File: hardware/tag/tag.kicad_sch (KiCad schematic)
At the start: 108 parts, among them J1 USB_C_Receptacle_USB2.0_16P, J2 BATTERY, J3 UART, J4 I2C, J5 STM SWD, J7 BLE SWD, J8 SOURCE, SW1 RESET, SW2 BOOT, SW3 USER, U1 ICM-45686, U2 TPS63070RNMR, U3 BQ24075RGT, U4 USBLC6-2SC6, U5 FSC-BT630, U6 STM32F411CEUx, U7 DWM1000, Y1 NX3215SA-32.768kHz(DNP), Y2 NX3225SA-24MHz

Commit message: refactor(hw): iterate on tag rev 0.2 design
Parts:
- removed C15: DNP, Capacitor_SMD:C_0805_2012Metric_Pad1.18x1.45mm_HandSolder, symbol Device:C
- removed C5: 1u, Capacitor_SMD:C_0805_2012Metric_Pad1.18x1.45mm_HandSolder, symbol Device:C
- removed C6, C7: 4.7u, Capacitor_SMD:C_0805_2012Metric_Pad1.18x1.45mm_HandSolder, symbol Device:C
- removed D1: RED, LED_SMD:LED_0603_1608Metric_Pad1.05x0.95mm_HandSolder, symbol Device:LED
- removed D2: YELLOW, LED_SMD:LED_0603_1608Metric_Pad1.05x0.95mm_HandSolder, symbol Device:LED
- removed R18, R9: 6k, Resistor_SMD:R_0603_1608Metric_Pad0.98x0.95mm_HandSolder, symbol Device:R
- removed R8: 10k, Resistor_SMD:R_0603_1608Metric_Pad0.98x0.95mm_HandSolder, symbol Device:R
- removed SW2: BOOT, Button_Switch_SMD:SW_SPDT_PCM12, symbol Switch:SW_SPDT
- removed U3: BQ24075RGT, Package_DFN_QFN:VQFN-16-1EP_3x3mm_P0.5mm_EP1.6x1.6mm, symbol Battery_Management:BQ24075RGT
- removed U5: FSC-BT630, Other_Footprint:FSC-BT630, symbol FSC-BT630_Generic_20P:FSC-BT630_Named_20P
- added C10: 1u, Capacitor_SMD:C_0805_2012Metric_Pad1.18x1.45mm_HandSolder, symbol Device:C
- added C12, C8: DNP, Capacitor_SMD:C_01005_0402Metric, symbol Device:C_Small
- added C34: 47n, Capacitor_SMD:C_0603_1608Metric, symbol Device:C_Small
- added C35: 4.7u, Capacitor_SMD:C_0805_2012Metric, symbol Device:C_Small
- added C36: 20u, Capacitor_SMD:C_0805_2012Metric, symbol Device:C
- added C37: 10u, Capacitor_SMD:C_0805_2012Metric, symbol Device:C
- added D9: YELLOW, LED_SMD:LED_0603_1608Metric_Pad1.05x0.95mm_HandSolder, symbol Device:LED
- added J6: BLE_Conn, Connector_Coaxial:U.FL_Hirose_U.FL-R-SMT-1_Vertical, symbol Connector:Conn_Coaxial_Small
- added L2: DNP, Inductor_SMD:L_0402_1005Metric, symbol Device:L
- added L3: 1u, Inductor_SMD:L_Sunlord_SWPA4020S, symbol Device:L
- added R25: 2.2k, Resistor_SMD:R_0603_1608Metric_Pad0.98x0.95mm_HandSolder, symbol Device:R
- added R26: 10K, Resistor_SMD:R_0603_1608Metric_Pad0.98x0.95mm_HandSolder, symbol Device:R
- added R27: DNP, Resistor_SMD:R_0603_1608Metric_Pad0.98x0.95mm_HandSolder, symbol Device:R
- added SW2: PWR, Button_Switch_SMD:SW_Push_1P1T-MP_NO_Horizontal_Alps_SKRTLAE010, symbol Switch:SW_Push
- added U5: FSC-BT630, other_footprint:FSC-BT630, symbol FSC-BT630:FSC-BT630_Named_20P
- added U8: BQ25628RYKR, Other_Footprint:IC_BQ25628RYKR, symbol BQ25628RYKR:BQ25628RYKR
- D3: value YELLOW -> GREEN
- D4: value GREEN -> RED
- R2: value 3.1k -> 10k
- R3: value 3.56k -> 10k
- renumbered C14 to C15
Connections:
- net +3.3V: now also R2.1, R3.1, U5.7 (VDD)
- net +BATT: now also C37.1, U8.8 (BAT)
- net BLE_RST: now also U5.6 (RESET)
- net BLE_RX: now also U5.1 (UART_TX)
- net BLE_SWDCLK: now also U5.9 (SWDCLK)
- net BLE_SWDIO: now also U5.10 (SWDIO)
- net BLE_TX: now also U5.2 (UART_RX)
- net GND: now also R14.1, C10.1, C12.2, C35.2, C36.2, C37.2, C8.2, D9.1 (K), J6.2 (Ext), R27.1, SW2.1, U5.19 (GND1), U5.8 (GND0), U8.14 (~{CE}), U8.15 (GND); no longer R2.2, R3.2
- net SYS: now also C36.1, L3.2, U8.9 (SYS)
- net VBUS: now also C10.2, U8.18 (VBUS)
- net at R19.2: now also U5.15 (P0.03)
- net PA15 / TIM2_CH1 renamed LED_PM
- net LED_PM: now also R25.2
- net PA8 / TIM1_CH1 renamed PM_SCL
- net PM_SCL: now also R2.2, U8.13 (SCL)
- net PB4/TIM3_CH1 renamed PM_SDA
- net PM_SDA: now also R3.2, U8.12 (SDA)
- net PB6 / TIM4_CH1: no longer names the net of U6.42 (PB6)
- new net: C8.1, J6.1 (In), L2.2
- new net: R26.1, SW2.2
- new net: R26.2, U8.7 (~{QON})
- new net: D9.2 (A), R25.1
- new net: R27.2, U8.4 (ILIM/D-)
- new net: C35.1, U8.2 (REGN)
- new net: C34.2, L3.1, U8.16 (SW)
- new net: C12.1, L2.1, U5.20 (EXT_ANT)
- new net: C34.1, U8.1 (BTST)
- new net STAT: U8.10 (STAT)
- new net TS: U8.5 (TS_BIAS/D+), U8.6 (TS)
- no-connect marks 31 -> 33
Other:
- note added: "PI Filter"
- note added: "TRACE 50 Ohm !"
- moved on the sheet: C16, C17, C18, C19, C20, C21, C22, C23, C24, C25, C26, C27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

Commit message: update(hw): release tag revision 0.2
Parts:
- removed C1: 10u, Capacitor_SMD:C_0805_2012Metric_Pad1.18x1.45mm_HandSolder, symbol Device:C
- removed C10: 1u, Capacitor_SMD:C_0805_2012Metric_Pad1.18x1.45mm_HandSolder, symbol Device:C
- removed C34: 47n, Capacitor_SMD:C_0603_1608Metric, symbol Device:C_Small
- removed C35: 4.7u, Capacitor_SMD:C_0805_2012Metric, symbol Device:C_Small
- removed C36: 20u, Capacitor_SMD:C_0805_2012Metric, symbol Device:C
- removed C37: 10u, Capacitor_SMD:C_0805_2012Metric, symbol Device:C
- removed L3: 1u, Inductor_SMD:L_Sunlord_SWPA4020S, symbol Device:L
- removed R2, R3: 10k, Resistor_SMD:R_0603_1608Metric_Pad0.98x0.95mm_HandSolder, symbol Device:R
- removed R27: DNP, Resistor_SMD:R_0603_1608Metric_Pad0.98x0.95mm_HandSolder, symbol Device:R
- removed SW2: PWR, Button_Switch_SMD:SW_Push_1P1T-MP_NO_Horizontal_Alps_SKRTLAE010, symbol Switch:SW_Push
- removed U8: BQ25628RYKR, Other_Footprint:IC_BQ25628RYKR, symbol BQ25628RYKR:BQ25628RYKR
- added C4: 100n, Capacitor_SMD:C_0603_1608Metric_Pad1.08x0.95mm_HandSolder, symbol Device:C
- added C6: 1u, Capacitor_SMD:C_0805_2012Metric_Pad1.18x1.45mm_HandSolder, symbol Device:C
- added C7: 1u, Capacitor_SMD:C_0603_1608Metric_Pad1.08x0.95mm_HandSolder, symbol Device:C
- added C8: 4.7u, Capacitor_SMD:C_0805_2012Metric_Pad1.18x1.45mm_HandSolder, symbol Device:C
- added C9: 10u, Capacitor_SMD:C_0805_2012Metric_Pad1.18x1.45mm_HandSolder, symbol Device:C
- added J9: I2C, Other_Footprint:JST_BM04B-SRSS-TB_LF__SN_, symbol BM04B-SRSS-TB_LF__SN_:BM04B-SRSS-TB_LF__SN_
- added Q1: AO664, Package_SO:TSOP-6_1.65x3.05mm_P0.95mm, symbol Transistor_FET:IRF7309PBF
- added R12: 100k, Resistor_SMD:R_0603_1608Metric_Pad0.98x0.95mm_HandSolder, symbol Device:R
- added R13, R8: 10k, Resistor_SMD:R_0603_1608Metric_Pad0.98x0.95mm_HandSolder, symbol Device:R
- added R5: 3.1k, Resistor_SMD:R_0603_1608Metric_Pad0.98x0.95mm_HandSolder, symbol Device:R
- added R6: 3.56k, Resistor_SMD:R_0603_1608Metric_Pad0.98x0.95mm_HandSolder, symbol Device:R
- added SW1: PWR, Button_Switch_SMD:SW_Push_1P1T-MP_NO_Horizontal_Alps_SKRTLAE010, symbol Switch:SW_Push_Shielded
- added U1: MAX17048G_T10, Package_SON:SON-8-1EP_3x2mm_P0.5mm_EP1.4x1.6mm, symbol MAX17048G_T10:MAX17048G_T10
- added U5: BQ24075RGT, Package_DFN_QFN:VQFN-16-1EP_3x3mm_P0.5mm_EP1.6x1.6mm, symbol Battery_Management:BQ24075RGT
- D3: value GREEN -> YELLOW
- D4: renamed from D9; value YELLOW -> GREEN
- D5: renamed from D4; value RED -> GREEN
- R14: value 10K -> 10k
- TP2: renamed from TP3; footprint TestPoint:TestPoint_Pad_D2.0mm -> TestPoint:TestPoint_Pad_1.5x1.5mm
- TP5: renamed from TP4; footprint TestPoint:TestPoint_Pad_D2.0mm -> TestPoint:TestPoint_Pad_1.5x1.5mm
- renumbered C2 to C1, C31 to C10, C13 to C12, C32 to C13, C15 to C14, C33 to C15, C27 to C16, C26 to C17, C16 to C18, C17 to C19, C3 to C2, C18 to C20, C19 to C21, C20 to C22, C21 to C23, C22 to C24, C12 to C25, C8 to C26, C23 to C27, C24 to C28, C25 to C29, C4 to C3, C28 to C30, C29 to C31, C30 to C32, C9 to C5, D7 to D1, D8 to D2, D5 to D6, D6 to D7, H3 to H1, H4 to H2, H2 to H3, H1 to H4, J6 to J3, J8 to J4, J4 to J6, J3 to J7, J7 to J8, R4 to R1, R11 to R10, R12 to R11, R13 to R15, R19 to R16, R16 to R18, R25 to R19, R5 to R2, R15 to R20, R1 to R21, R20 to R22, R21 to R23, R22 to R25, R7 to R3, R6 to R4, R23 to R7, R10 to R9, SW1 to SW2, TP8 to TP10, TP9 to TP11, TP14 to TP12, TP10 to TP13, TP11 to TP14, TP5 to TP15, TP6 to TP3, TP12 to TP4, TP2 to TP6, TP15 to TP7, TP13 to TP8, TP7 to TP9, U4 to U2, U1 to U3, U2 to U4, U5 to U6, U6 to U7, U7 to U8
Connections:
- net +3.3V: now also J5.4, J8.5, J9.1; no longer J5.1, J8.1
- net +BATT: now also C4.1, C8.1, U1.3 (VDD), U5.2 (BAT), U5.3 (BAT)
- net BLE_RST: now also J8.3; no longer J8.4
- net BLE_SWDCLK: now also J8.1; no longer J8.3
- net GND: now also J5.3, J6.2, J7.2, J8.4, R26.2, C4.2, C6.1, C7.1, C8.2, C9.2, J9.2, J9.S1 (SHIELD), J9.S2 (SHIELD), Q1.5 (S1), R5.2, R6.2, R8.1, SW1.MP (B), U1.1 (CTG), U1.4 (GND), U1.6 (QSTRT), U1.9 (EP), U5.15 (SYSOFF), U5.17 (VSS), U5.4 (~{CE}), U5.6 (EN1), U5.8 (VSS); no longer J5.4, J6.4, J7.4, J8.5, R14.1
- net PA10 / UART1_RX: now also J7.3; no longer J7.2
- net PA9 / UART1_TX: now also J7.4; no longer J7.3
- net PB0 / ADC_IN8: now also J9.4
- net PB1 / ADC_IN9: now also J9.3
- net PB8 / I2C1_SCL: now also J6.3, U1.7 (SCL); no longer J6.2
- net PB9 / I2C1_SDA: now also J6.4, U1.8 (SDA); no longer J6.3
- net STM_SWDCLK: now also J5.1; no longer J5.2
- net STM_SWDIO: now also J5.2; no longer J5.3
- net SYS: now also C9.1, Q1.2 (S2), R13.2, U5.10 (OUT), U5.11 (OUT), U5.5 (EN2); no longer C1.1, C2.1, C3.1, R1.2, R2.2, U4.12_13 (VIN)
- net VBUS: now also C6.2, U5.13 (IN)
- net at R26.1: now also U7.44 (BOOT0)
- net LOAD: now reaches R14.2
- net LOAD: now also C1.1, C2.1, C3.1, R1.2, R2.2, U4.12_13 (VIN), Q1.4 (D2); no longer U7.44 (BOOT0)
- new net: C7.2, R12.1, SW1.1
- new net: Q1.3 (G2), Q1.6 (S1), R12.2, R13.1
- new net: Q1.1 (G1), R14.1, SW1.2
- new net: R8.2, U5.1 (TS)
- new net: R5.1, U5.12 (ILIM)
- new net: R6.1, U5.16 (ISET)
- no-connect marks 33 -> 35
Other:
- note added: "AO664"
- moved on the sheet: C16, C17, C18, C19, C20, C21, C22, C23, C24, C25, C26, C27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

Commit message: wip
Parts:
- added F1: Polyfuse_Small, Fuse:Fuse_1206_3216Metric, symbol Device:Polyfuse_Small
- C25, C26: footprint Capacitor_SMD:C_01005_0402Metric -> Capacitor_SMD:C_0402_1005Metric
- renumbered F1 to F2
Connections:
- net VBUS: now also F1.1; no longer C6.2, U5.13 (IN)
- new net VBUS_PROTECT: C6.2, F1.2, U5.13 (IN)
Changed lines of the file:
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@@
 	(wire
 		(pts
+			(xy 93.98 153.67) (xy 93.98 154.94)
+		)
+		(stroke
+			(width 0)
+			(type default)
+		)
+	)
+	(wire
+		(pts
 			(xy 179.07 222.25) (xy 179.07 237.49)
 		)
@@
 	(wire
 		(pts
-			(xy 93.98 165.1) (xy 93.98 170.18)
-		)
-		(stroke
-			(width 0)
-			(type default)
-		)
-	)
-	(wire
-		(pts
 			(xy 382.27 220.98) (xy 391.16 220.98)
 		)
@@
 	(wire
 		(pts
+			(xy 93.98 160.02) (xy 93.98 170.18)
+		)
+		(stroke
+			(width 0)
+			(type default)
+		)
+	)
+	(wire
+		(pts
 			(xy 127 212.09) (xy 127 215.9)
 		)
@@
 		)
 	)
+	(label "VBUS_PROTECT"
+		(at 93.98 170.18 90)
+		(effects
+			(font
+				(size 0.9652 0.9652)
+			)
+			(justify left bottom)
+		)
+	)
 	(label "SPI_MOSI"
 		(at 121.92 57.15 180)
@@
 		)
 	)
+	(label "VBUS_PROTECT"
+		(at 111.76 214.63 90)
+		(effects
+			(font
+				(size 0.9652 0.9652)
+			)
+			(justify left bottom)
+		)
+	)
 	(label "BLE_SWDCLK"
 		(at 382.27 220.98 0)
@@
 			)
 		)
-		(property "Footprint" "Capacitor_SMD:C_01005_0402Metric"
+		(property "Footprint" "Capacitor_SMD:C_0402_1005Metric"
 			(at 266.7 55.88 0)
 			(effects
@@
 	)
 	(symbol
+		(lib_id "Device:Polyfuse_Small")
+		(at 93.98 157.48 0)
+		(unit 1)
+		(exclude_from_sim no)
+		(in_bom yes)
+		(on_board yes)
+		(dnp no)
+		(property "Reference" "F1"
+			(at 96.52 156.2099 0)
+			(effects
+				(font
+					(size 1.27 1.27)
+				)
+				(justify left)
+			)
+		)
+		(property "Value" "Polyfuse_Small"
+			(at 96.52 158.7499 0)
+			(effects
+				(font
+					(size 1.27 1.27)
+				)
+				(justify left)
+			)
+		)
+		(property "Footprint" "Fuse:Fuse_1206_3216Metric"
+			(at 95.25 162.56 0)
+			(effects
+				(font
+					(size 1.27 1.27)
+				)
+				(justify left)
+				(hide yes)
+			)
+		)
+		(property "Datasheet" "~"
+			(at 93.98 157.48 0)
+			(effects
+				(font
+					(size 1.27 1.27)
+				)
+				(hide yes)
+			)
+		)
+		(property "Description" "Resettable fuse, polymeric positive temperature coefficient, small symbol"
+			(at 93.98 157.48 0)
+			(effects
+				(font
+					(size 1.27 1.27)
+				)
+				(hide yes)
+			)
+		)
+		(pin "2"
+		)
+		(pin "1"
+		)
+		(instances
+			(project "tag"
+				(path "/36ff3ade-5474-48a6-a94c-a185611a6890"
+					(reference "F1")
+					(unit 1)
+				)
+			)
+		)
+	)
+	(symbol
 		(lib_id "power:+3.3V")
 		(at 144.78 95.25 0)
@@
 			)
 		)
-		(property "Footprint" "Capacitor_SMD:C_01005_0402Metric"
+		(property "Footprint" "Capacitor_SMD:C_0402_1005Metric"
 			(at 251.46 55.88 0)
 			(effects
@@
 	)
 	(symbol
-		(lib_id "power:VBUS")
-		(at 111.76 214.63 0)
-		(unit 1)
-		(exclude_from_sim no)
-		(in_bom yes)
-		(on_board yes)
-		(dnp no)
-		(property "Reference" "#PWR024"
-			(at 111.76 218.44 0)
-			(effects
-				(font
-					(size 1.27 1.27)
-				)
-				(hide yes)
-			)
-		)
-		(property "Value" "VBUS"
-			(at 112.014 210.566 0)
-			(effects
-				(font
-					(size 1.27 1.27)
-				)
-			)
-		)
-		(property "Footprint" ""
-			(at 111.76 214.63 0)
-			(effects
-				(font
-					(size 1.27 1.27)
-				)
-				(hide yes)
-			)
-		)
-		(property "Datasheet" ""
-			(at 111.76 214.63 0)
-			(effects
-				(font
-					(size 1.27 1.27)
-				)
-				(hide yes)
-			)
-		)
-		(property "Description" "Power symbol creates a global label with name \"VBUS\""
-			(at 111.76 214.63 0)
-			(effects
-				(font
-					(size 1.27 1.27)
-				)
-				(hide yes)
-			)
-		)
-		(pin "1"
-		)
-		(instances
-			(project "learningkcad"
-				(path "/36ff3ade-5474-48a6-a94c-a185611a6890"
-					(reference "#PWR024")
-					(unit 1)
-				)
-			)
-		)
-	)
-	(symbol
 		(lib_id "power:GND")
 		(at 316.23 209.55 0)
@@
 	(symbol
 		(lib_id "power:VBUS")
-		(at 93.98 165.1 0)
+		(at 93.98 153.67 0)
 		(unit 1)
 		(exclude_from_sim no)
@@
 		(dnp no)
 		(property "Reference" "#PWR017"
-			(at 93.98 168.91 0)
+			(at 93.98 157.48 0)
 			(effects
 				(font
@@
 		)
 		(property "Value" "VBUS"
-			(at 94.234 160.274 0)
+			(at 94.234 148.844 0)
 			(effects
 				(font
@@
 		)
 		(property "Footprint" ""
-			(at 93.98 165.1 0)
+			(at 93.98 153.67 0)
 			(effects
 				(font
@@
 		)
 		(property "Datasheet" ""
-			(at 93.98 165.1 0)
+			(at 93.98 153.67 0)
 			(effects
 				(font
@@
 		)
 		(property "Description" "Power symbol creates a global label with name \"VBUS\""
-			(at 93.98 165.1 0)
+			(at 93.98 153.67 0)
 			(effects
 				(font
@@
 		(on_board yes)
 		(dnp no)
-		(property "Reference" "F1"
+		(property "Reference" "F2"
 			(at 314.96 40.6399 0)
 			(effects
@@
 			(project "tag"
 				(path "/36ff3ade-5474-48a6-a94c-a185611a6890"
-					(reference "F1")
+					(reference "F2")
 					(unit 1)
 				)

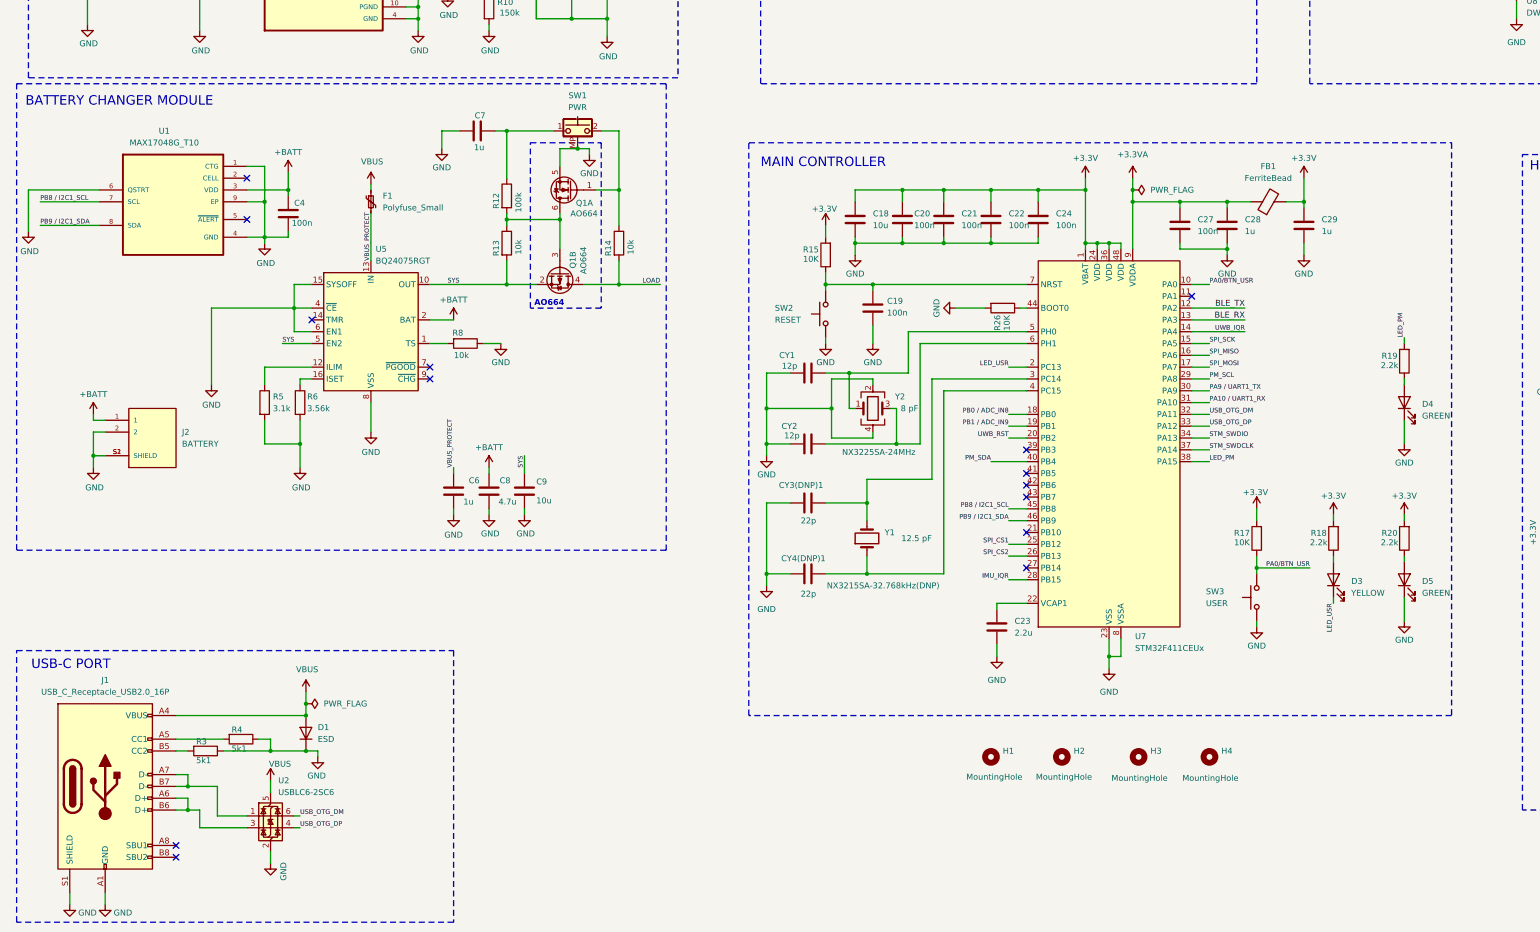
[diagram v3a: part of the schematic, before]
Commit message: update(hw): add schottky diode to prevent reverse current between USB and 5V header
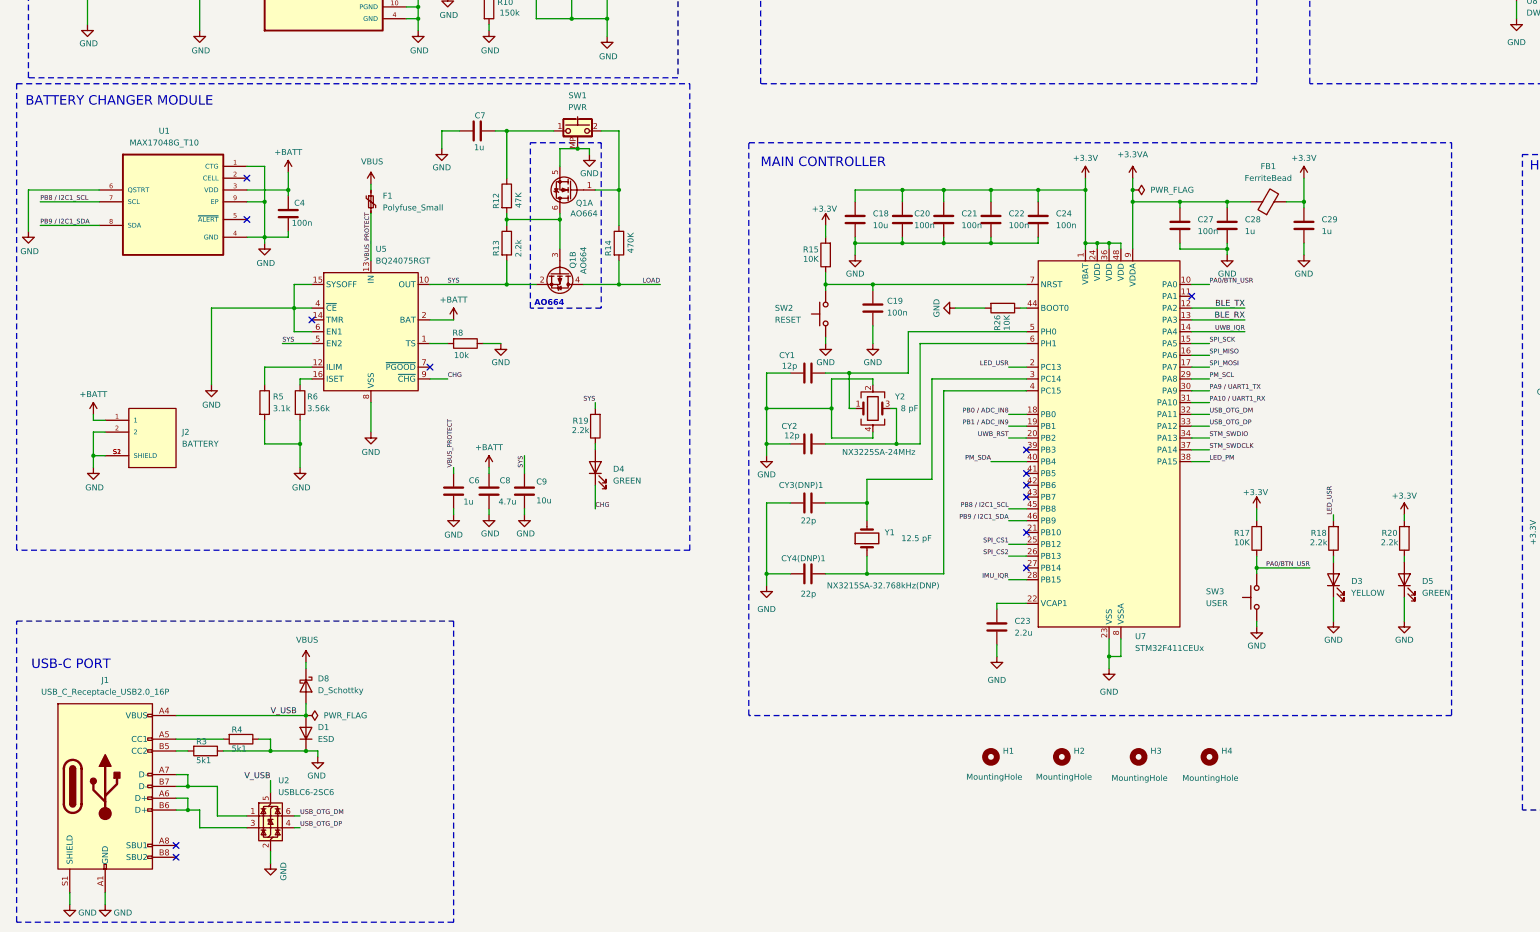
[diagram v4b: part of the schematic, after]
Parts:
- added D8: D_Schottky, Diode_SMD:D_SOD-123F, symbol Device:D_Schottky
- R12: value 100k -> 47K
- R13: value 10k -> 2.2k
- R14: value 10k -> 470K
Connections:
- net +3.3V: no longer R18.2
- net GND: now also D3.1 (K); no longer D4.1 (K)
- net LED_PM: no longer R19.2
- net LED_USR: now also R18.2; no longer D3.1 (K)
- net SYS: now also R19.2
- net VBUS: now also D8.1 (K); no longer D1.2 (A), J1.A4 (VBUS), J1.A9 (VBUS), J1.B4 (VBUS), J1.B9 (VBUS), U2.5 (VBUS)
- net CHG: now reaches U5.9 (~{CHG})
- net CHG: now also D4.1 (K)
- new net V_USB: D1.2 (A), D8.2 (A), J1.A4 (VBUS), J1.A9 (VBUS), J1.B4 (VBUS), J1.B9 (VBUS), U2.5 (VBUS)
- no-connect marks 35 -> 34
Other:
- moved on the sheet: D4, R19

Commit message: wip
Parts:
- TP10, TP11, TP12, TP13, TP14, TP15, TP4, TP9: footprint TestPoint:TestPoint_Pad_D1.0mm -> TestPoint:TestPoint_Pad_D1.5mm
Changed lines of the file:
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@@
 			)
 		)
-		(property "Footprint" "TestPoint:TestPoint_Pad_D1.0mm"
+		(property "Footprint" "TestPoint:TestPoint_Pad_D1.5mm"
 			(at 439.42 205.74 0)
 			(effects
@@
 			)
 		)
-		(property "Footprint" "TestPoint:TestPoint_Pad_D1.0mm"
+		(property "Footprint" "TestPoint:TestPoint_Pad_D1.5mm"
 			(at 439.42 227.33 0)
 			(effects
@@
 			)
 		)
-		(property "Footprint" "TestPoint:TestPoint_Pad_D1.0mm"
+		(property "Footprint" "TestPoint:TestPoint_Pad_D1.5mm"
 			(at 449.58 161.29 0)
 			(effects
@@
 			)
 		)
-		(property "Footprint" "TestPoint:TestPoint_Pad_D1.0mm"
+		(property "Footprint" "TestPoint:TestPoint_Pad_D1.5mm"
 			(at 450.85 205.74 0)
 			(effects
@@
 			)
 		)
-		(property "Footprint" "TestPoint:TestPoint_Pad_D1.0mm"
+		(property "Footprint" "TestPoint:TestPoint_Pad_D1.5mm"
 			(at 412.75 227.33 0)
 			(effects
@@
 			)
 		)
-		(property "Footprint" "TestPoint:TestPoint_Pad_D1.0mm"
+		(property "Footprint" "TestPoint:TestPoint_Pad_D1.5mm"
 			(at 436.88 184.15 0)
 			(effects
@@
 			)
 		)
-		(property "Footprint" "TestPoint:TestPoint_Pad_D1.0mm"
+		(property "Footprint" "TestPoint:TestPoint_Pad_D1.5mm"
 			(at 450.85 184.15 0)
 			(effects
@@
 			)
 		)
-		(property "Footprint" "TestPoint:TestPoint_Pad_D1.0mm"
+		(property "Footprint" "TestPoint:TestPoint_Pad_D1.5mm"
 			(at 435.61 161.29 0)
 			(effects
